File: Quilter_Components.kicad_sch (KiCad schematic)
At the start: 44 parts, among them J1 Conn_01x10_Male, J2 Conn_01x10_Male, J3 Conn_01x10_Male, J4 Eurorack_10_pin_power, U1 TL072, U2 TL074, U3 TL074, U4 TL074

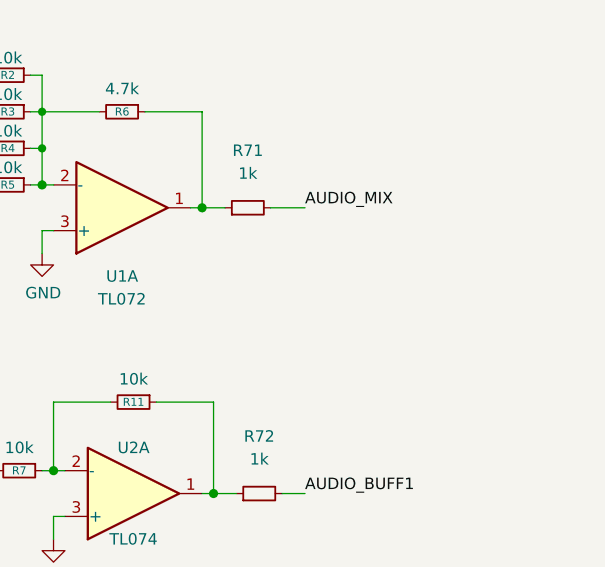
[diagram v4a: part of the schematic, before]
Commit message: Updated to Kicad 7
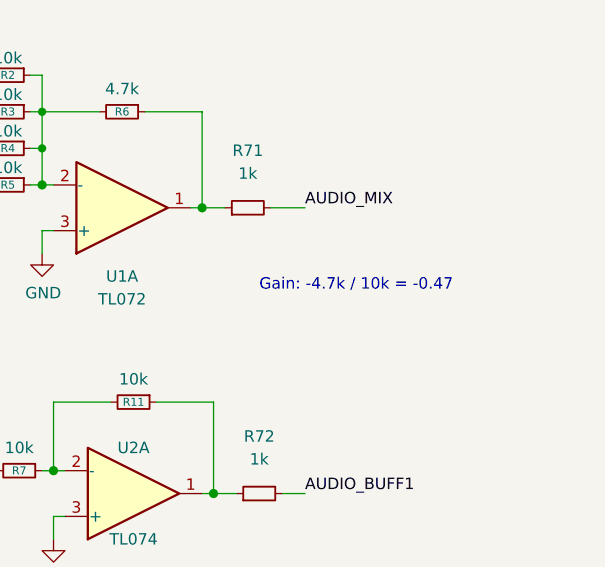
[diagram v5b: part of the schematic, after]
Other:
- note added: "Gain: -4.7k / 10k = -0.47"
